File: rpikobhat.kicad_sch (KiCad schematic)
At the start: 34 parts

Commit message: Mostly done.  Need to check gerbers.
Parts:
- removed D4: (no value), symbol Diode:1N914WT
- removed J3: (no value), symbol raspberrypi_hat:OX40HAT
- removed Q3: (no value), symbol rpikobhat-rescue:2N7002P_215-dk_Transistors-FETs-MOSFETs-Single
- added C2: 10uf, symbol Device:C_Polarized_US
- added D4, D5: 1N4004, Diode_SMD:D_SMB_Handsoldering, symbol Diode:1N4004
- added J2, J4, J5: Screw_Terminal_01x02, TerminalBlock_Philmore:TerminalBlock_Philmore_TB132_1x02_P5.00mm_Horizontal, symbol Connector:Screw_Terminal_01x02
- added J3: PI40HAT, Connector_PinSocket_2.54mm:PinSocket_2x20_P2.54mm_Vertical, symbol raspberrypi_hat:PI40HAT
- added Q3: (no value), symbol Transistor_FET:IRFS4321
- added R12: R_US, Resistor_SMD:R_1206_3216Metric_Pad1.30x1.75mm_HandSolder, symbol Device:R_US
- added R13: 20.0k, Resistor_SMD:R_1206_3216Metric_Pad1.30x1.75mm_HandSolder, symbol Device:R_US
- C1: value (none) -> 0.1u
- D1, D3: value (none) -> MBR0560LT1G; footprint (none) -> Diode_SMD:D_SOD-123
- H1, H2, H3, H4: value (none) -> 3mm_Mounting_Hole; footprint (none) -> project_footprints:NPTH_3mm_ID
- J1: value (none) -> Conn_Coaxial_Power; footprint (none) -> Connector_BarrelJack:BarrelJack_CUI_PJ-036AH-SMT_Horizontal
- J6: value (none) -> CONN_02X02; footprint (none) -> Connector_PinHeader_2.54mm:PinHeader_2x02_P2.54mm_Vertical
- J9: value (none) -> CONN_01X02; footprint (none) -> Connector_PinHeader_2.54mm:PinHeader_1x02_P2.54mm_Vertical
- Q1: value (none) -> DMG2305UX; footprint (none) -> Package_TO_SOT_SMD:SOT-23
- Q2: value (none) -> DMMT5401; footprint (none) -> Package_TO_SOT_SMD:SOT-23-6
- R1, R10, R2, R3: value (none) -> 20.0k; footprint (none) -> Resistor_SMD:R_1206_3216Metric_Pad1.30x1.75mm_HandSolder
- R11, R7, R9: value (none) -> DNP; footprint (none) -> Resistor_SMD:R_0603_1608Metric_Pad0.84x1.00mm_HandSolder
- R23, R29: value (none) -> 10K; footprint (none) -> Resistor_SMD:R_0603_1608Metric_Pad0.84x1.00mm_HandSolder
- R24: value (none) -> 47K; footprint (none) -> Resistor_SMD:R_0603_1608Metric_Pad0.84x1.00mm_HandSolder
- R4, R5: value (none) -> R_US; footprint (none) -> Resistor_THT:R_Axial_DIN0414_L11.9mm_D4.5mm_P25.40mm_Horizontal
- R6, R8: value (none) -> 3.9K; footprint (none) -> Resistor_SMD:R_0603_1608Metric_Pad0.84x1.00mm_HandSolder
- U1: value (none) -> LM393DR; footprint (none) -> Package_DIP:DIP-8_W7.62mm
- U2: value (none) -> CAT24C32; footprint (none) -> Package_SOIC:SOIC-8_3.9x4.9mm_P1.27mm
- U3: value (none) -> Key
- U4: value (none) -> Sounder
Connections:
- net GND: now also C2.2, D4.1 (K), D5.2 (A), J3.14 (GND), J3.20 (GND), J3.25 (GND), J3.30 (GND), J3.34 (GND), J3.39 (GND), J3.6 (GND), J3.9 (GND), Q3.3 (S), R12.2
- net GPI21: now also J3.40 (BCM21)
- net GPO26: now also J3.37 (BCM26)
- net ID_SC_EEPROM: now also J3.28 (BCM1)
- net ID_SD_EEPROM: now also J3.27 (BCM0)
- net LOOP_STATE: now also J2.2 (Pin_2), R13.1
- net P3V3_HAT: now also U1.8 (VCC), J3.1 (P3V3)
- net P5V_HAT: now also R3.1, J3.2 (P5V), J3.4 (P5V); no longer U1.8 (VCC)
- net at R2.1, U1.7 (2OUT): now also Q3.1 (G)
- net at D3.1 (K): now also Q3.2 (D), R13.2
- net at R10.2, U1.3: now also D4.2 (A)
- net at R4.1, R5.1, U3.2 (KEY): now also J2.1 (Pin_1), J5.2 (Pin_2)
- net at D1.1 (K), D2.2 (A): now also R12.1
- net at U3.1 (KEY), U4.2 (SND): now also J4.2 (Pin_2), J5.1 (Pin_1)
- net +5V: no longer names the net of C1.1, J1.1 (In), U4.1 (SND)
- net +5V: now also C2.1, D5.1 (K), J4.1 (Pin_1); no longer R3.1
- no-connect marks 0 -> 25
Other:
- note added: "4-150 OHM SOUNDER"
- note added: "KOB connects to J4-1 and J5-2."
- note added: "Key connects to J4."
- note added: "Key connects to J5."
- note added: "LM393 is a dual-comparator in 8 pin DIP."
- note added: "Loop Resistor goes here."
- note added: "Loop State is HIGH when telegraph circuit is closed."
- note added: "Loop State is also high when telegraph circuit is opened on the remote side of the circuit."
- note added: "Loop voltage supply plugs in here."
- note added: "MORSE KOB HAT"
- note added: "Reverse Polarity Protect"
- note added: "Sounder connects to J4."
- note added: "The software must ignore GPI21 in this case."
- note added: "These resistors are"
- note added: "This capacitor must have appropriate"
- note added: "This part uses package TO-263-3."
- note added: "Use a device with 200V drain-to-source rating."
- note added: "Used screw terminals instead of binding posts. Just more practical."
- note added: "for permanent"
- note added: "installation."
- note added: "voltage rating."
- note removed: "4 OHM SOUNDER"
- note removed: "5V USB SUPPLY PLUGS IN HERE"
- note removed: "Binding posts here?"
- note removed: "Intent is to use surface mount SOT-23 for Q3"
- note removed: "Use the HAT 5V supply here, probably cleaner"
- moved on the sheet: C1, J1, R10, R2, R3, U1A, U1B, U4

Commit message: Added a few notes to schematic.
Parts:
- C1: footprint (none) -> Capacitor_SMD:C_1206_3216Metric_Pad1.33x1.80mm_HandSolder
- C2: footprint (none) -> Capacitor_THT:CP_Radial_D8.0mm_P5.00mm
- D2: value (none) -> MBR0560LT1G; footprint (none) -> Diode_SMD:D_SOD-123
- R12: value R_US -> (none); footprint Resistor_SMD:R_1206_3216Metric_Pad1.30x1.75mm_HandSolder -> (none)
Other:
- note added: "D2 NOT PLACED"
- note added: "R1 NOT PLACED"
- note added: "R13 NOT PLACED"
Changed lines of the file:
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@@
   (title_block
     (title "Raspberry Pi HAT")
-    (date "2021-11-08")
+    (date "2022-04-14")
     (rev "P1")
     (company "PiKOB Prototype Hat")
@@
     (effects (font (size 2 2) (thickness 0.4) bold) (justify left bottom))
   )
+  (text "R13 NOT PLACED" (at 266.7 167.64 0)
+    (effects (font (size 1.27 1.27)) (justify left bottom))
+  )
   (text "Use a device with 200V drain-to-source rating." (at 294.64 191.77 0)
     (effects (font (size 1.27 1.27)) (justify left bottom))
@@
   (text "4-150 OHM SOUNDER" (at 323.85 110.49 0)
     (effects (font (size 2.9972 2.9972) (thickness 0.5994) bold) (justify left bottom))
+  )
+  (text "D2 NOT PLACED" (at 167.005 203.835 0)
+    (effects (font (size 1.27 1.27)) (justify left bottom))
   )
   (text "Loop State is HIGH when telegraph circuit is closed."
@@
   )
   (text "SOUNDER DRIVER FROM GPO" (at 223.52 172.72 0)
+    (effects (font (size 1.27 1.27)) (justify left bottom))
+  )
+  (text "R1 NOT PLACED" (at 226.06 193.675 0)
     (effects (font (size 1.27 1.27)) (justify left bottom))
   )
@@
       (effects (font (size 1.27 1.27)) (justify left))
     )
-    (property "Footprint" "" (id 2) (at 296.8752 127 0)
+    (property "Footprint" "Capacitor_SMD:C_1206_3216Metric_Pad1.33x1.80mm_HandSolder" (id 2) (at 296.8752 127 0)
       (effects (font (size 1.27 1.27)) hide)
     )
@@
       (effects (font (size 1.27 1.27)) (justify left))
     )
-    (property "Footprint" "" (id 2) (at 242.57 123.19 0)
+    (property "Footprint" "Capacitor_THT:CP_Radial_D8.0mm_P5.00mm" (id 2) (at 242.57 123.19 0)
       (effects (font (size 1.27 1.27)) hide)
     )
@@
       (effects (font (size 1.27 1.27)) (justify left))
     )
-    (property "Value" "R_US" (id 1) (at 147.701 206.1722 0)
-      (effects (font (size 1.27 1.27)) (justify left))
-    )
-    (property "Footprint" "Resistor_SMD:R_1206_3216Metric_Pad1.30x1.75mm_HandSolder" (id 2) (at 147.066 204.724 90)
+    (property "Value" "" (id 1) (at 147.701 206.1722 0)
+      (effects (font (size 1.27 1.27)) (justify left))
+    )
+    (property "Footprint" "" (id 2) (at 147.066 204.724 90)
       (effects (font (size 1.27 1.27)) hide)
     )
@@
       (effects (font (size 1.27 1.27)) (justify right))
     )
-    (property "Value" "" (id 1) (at 163.322 205.613 90)
+    (property "Value" "MBR0560LT1G" (id 1) (at 163.322 205.613 90)
       (effects (font (size 1.27 1.27)) (justify right))
     )
-    (property "Footprint" "" (id 2) (at 165.735 204.47 0)
+    (property "Footprint" "Diode_SMD:D_SOD-123" (id 2) (at 165.735 204.47 0)
       (effects (font (size 1.27 1.27)) hide)
     )
@@
     )
     (path "/27ae7bb7-79c9-4ec7-94e4-30ebd7be8a24"
-      (reference "Q3") (unit 1) (value "IRFS4321") (footprint "Package_TO_SOT_SMD:TO-263-2")
+      (reference "Q3") (unit 1) (value "IRF640S") (footprint "Package_TO_SOT_SMD:TO-263-2")
     )
     (path "/00000000-0000-0000-0000-0000618f9856"
@@
     )
     (path "/7abec851-9a7e-4086-975b-7534dbf230ce"
-      (reference "R12") (unit 1) (value "R_US") (footprint "Resistor_SMD:R_1206_3216Metric_Pad1.30x1.75mm_HandSolder")
+      (reference "R12") (unit 1) (value "0 ohms") (footprint "Resistor_SMD:R_1206_3216Metric_Pad1.30x1.75mm_HandSolder")
     )
     (path "/f02c0157-bf91-4b1b-86c5-8385004b65df"

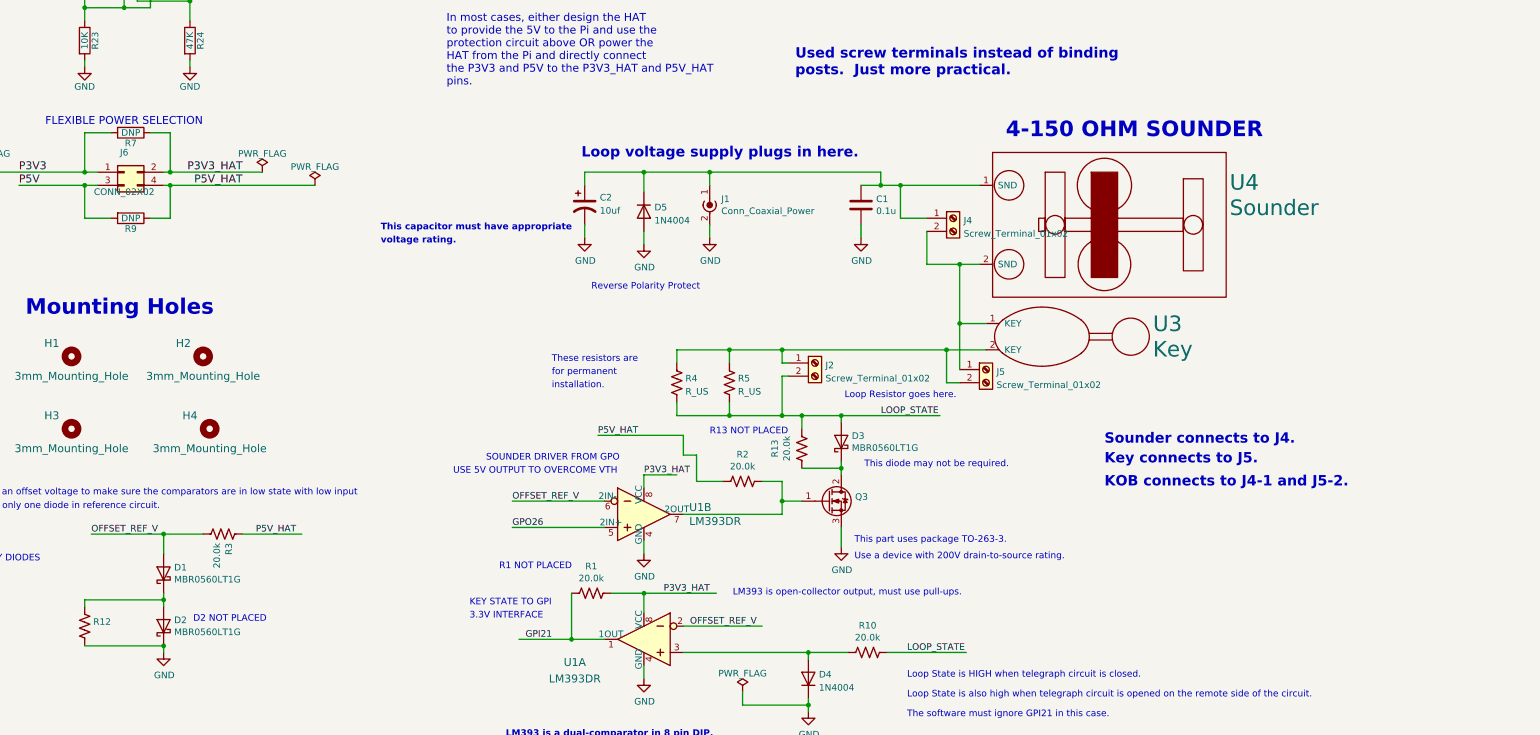
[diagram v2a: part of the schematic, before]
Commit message: Added snubber to sounder.
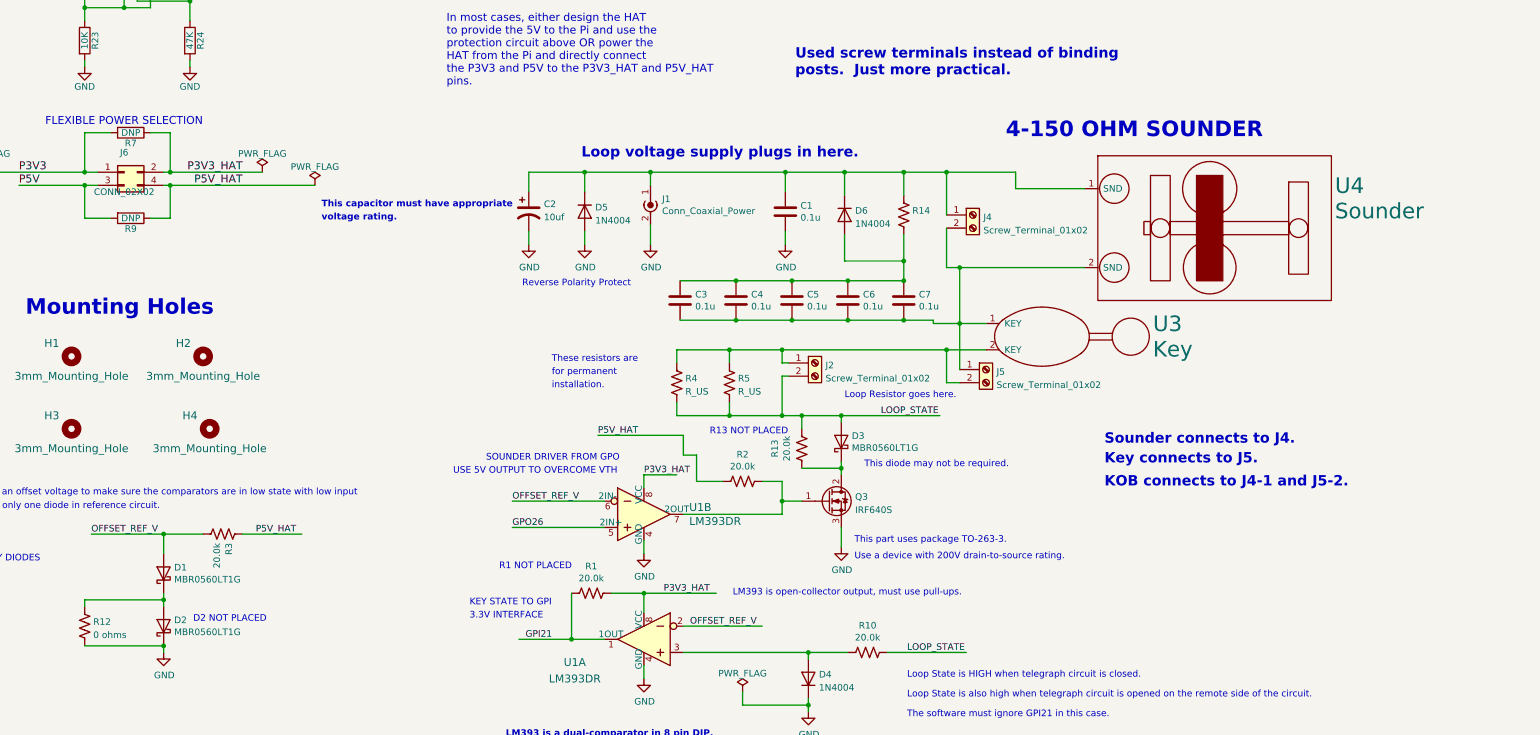
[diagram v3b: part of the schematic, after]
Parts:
- added C3, C4, C5, C6, C7: 0.1u, Capacitor_SMD:C_1206_3216Metric_Pad1.33x1.80mm_HandSolder, symbol Device:C
- added D6: 1N4004, Diode_SMD:D_SMB_Handsoldering, symbol Diode:1N4004
- added R14: (no value), symbol Device:R_US
- Q3: value (none) -> IRF640S; footprint (none) -> Package_TO_SOT_SMD:TO-263-2
- R12: value (none) -> 0 ohms; footprint (none) -> Resistor_SMD:R_1206_3216Metric_Pad1.30x1.75mm_HandSolder
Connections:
- net at J4.2 (Pin_2), J5.1 (Pin_1), U3.1 (KEY)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: now also C3.2, C4.2, C5.2, C6.2, C7.2
- net at C1.1, C2.1, D5.1 (K)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: now also D6.1 (K), R14.1
- new net: C3.1, C4.1, C5.1, C6.1, C7.1, D6.2 (A), R14.2
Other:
- moved on the sheet: C1, C2, D5, J1, J4, U4

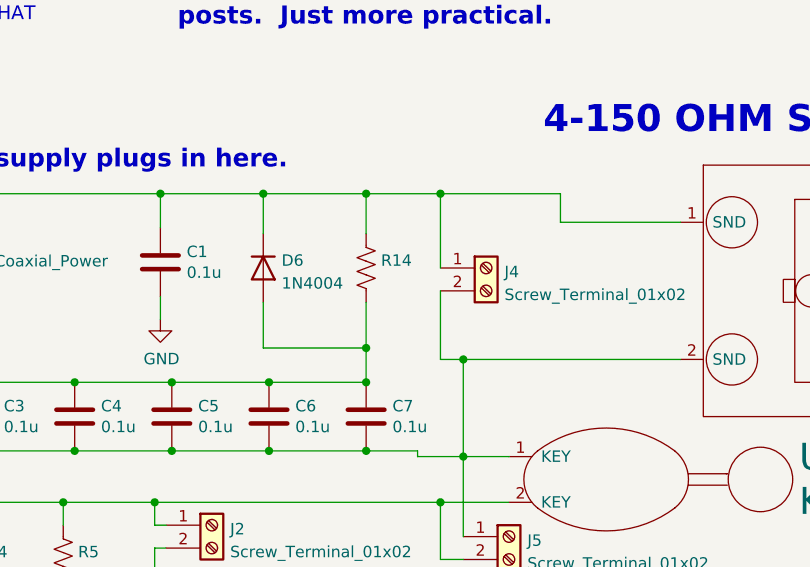
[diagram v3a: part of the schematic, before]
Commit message: Minor changes to notes on schematic.
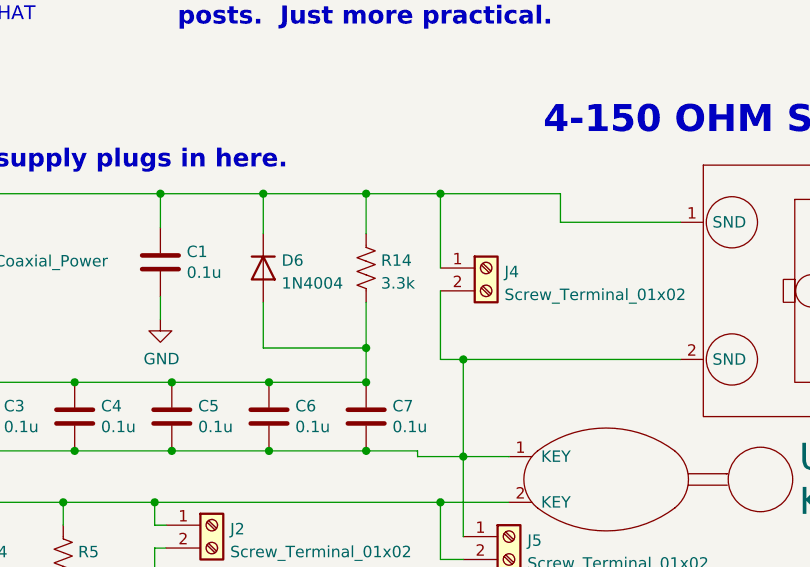
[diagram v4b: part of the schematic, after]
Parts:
- R14: value (none) -> 3.3k; footprint (none) -> Resistor_THT:R_Axial_DIN0414_L11.9mm_D4.5mm_P25.40mm_Horizontal
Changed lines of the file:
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@@
       (effects (font (size 1.27 1.27)) (justify left))
     )
-    (property "Value" "" (id 1) (at 305.816 126.7972 0)
+    (property "Value" "3.3k" (id 1) (at 305.816 126.7972 0)
       (effects (font (size 1.27 1.27)) (justify left))
     )
-    (property "Footprint" "" (id 2) (at 305.181 125.349 90)
+    (property "Footprint" "Resistor_THT:R_Axial_DIN0414_L11.9mm_D4.5mm_P25.40mm_Horizontal" (id 2) (at 305.181 125.349 90)
       (effects (font (size 1.27 1.27)) hide)
     )
